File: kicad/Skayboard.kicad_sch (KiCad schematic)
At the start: 13 parts, among them U1 ATmega32U4-M

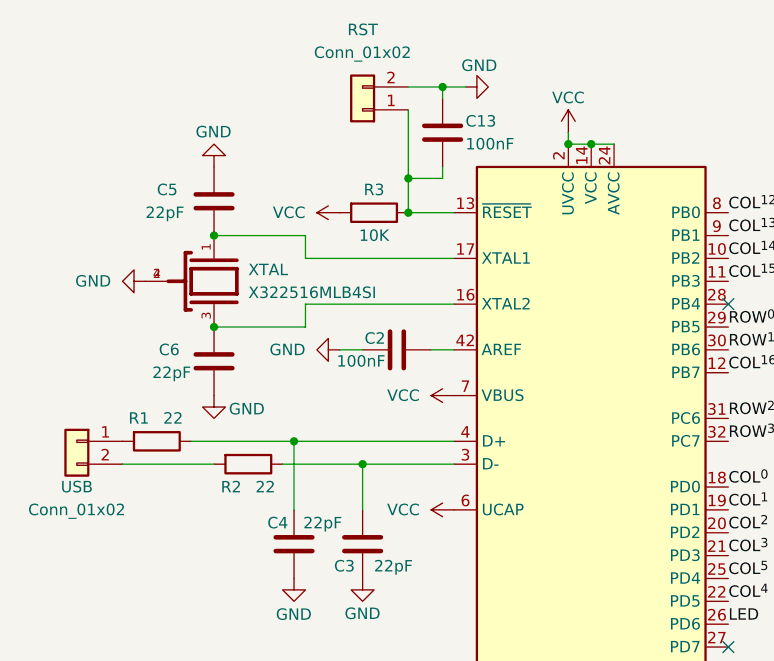
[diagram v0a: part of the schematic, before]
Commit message: fix: adds link for LEDs in README
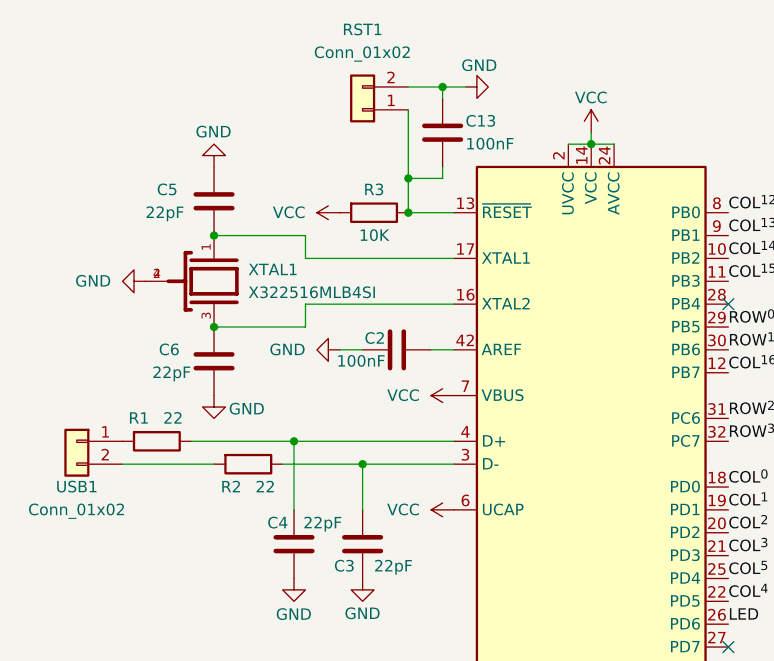
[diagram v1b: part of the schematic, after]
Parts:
- renumbered RST to RST1, USB to USB1, XTAL to XTAL1

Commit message: feat: finishes key layout
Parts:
- added POWER1: Conn_01x02, Connector_Wire:SolderWire-2.5sqmm_1x02_P7.2mm_D2.4mm_OD3.6mm, symbol Connector_Generic:Conn_01x02
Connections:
- net GND: now also POWER1.2 (Pin_2)
- net VCC: now also POWER1.1 (Pin_1)
- no-connect marks 3 -> 4
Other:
- added sheet " (inc/Skey.kicad_sch)
- added sheet , (inc/Skey.kicad_sch)
- added sheet - (inc/Skey.kicad_sch)
- added sheet . (inc/Skey.kicad_sch)
- added sheet 0 (inc/Skey.kicad_sch)
- added sheet 1 (inc/Skey.kicad_sch)
- added sheet 2 (inc/Skey.kicad_sch)
- added sheet 3 (inc/Skey.kicad_sch)
- added sheet 4 (inc/Skey.kicad_sch)
- added sheet 5 (inc/Skey.kicad_sch)
- added sheet 6 (inc/Skey.kicad_sch)
- added sheet 7 (inc/Skey.kicad_sch)
- added sheet 8 (inc/Skey.kicad_sch)
- added sheet 9 (inc/Skey.kicad_sch)
- added sheet ; (inc/Skey.kicad_sch)
- added sheet = (inc/Skey.kicad_sch)
- added sheet A (inc/Skey.kicad_sch)
- added sheet B (inc/Skey.kicad_sch)
- added sheet B Slash (inc/Skey.kicad_sch)
- added sheet Bksp (inc/Skey.kicad_sch)
- added sheet C (inc/Skey.kicad_sch)
- added sheet Caps (inc/Skey.kicad_sch)
- added sheet D (inc/Skey.kicad_sch)
- added sheet Del (inc/Skey.kicad_sch)
- added sheet Down (inc/Skey.kicad_sch)
- added sheet E (inc/Skey.kicad_sch)
- added sheet End (inc/Skey.kicad_sch)
- added sheet Enter (inc/Skey.kicad_sch)
- added sheet Esc (inc/Skey.kicad_sch)
- added sheet F (inc/Skey.kicad_sch)
- added sheet F Slash (inc/Skey.kicad_sch)
- added sheet G (inc/Skey.kicad_sch)
- added sheet H (inc/Skey.kicad_sch)
- added sheet Home (inc/Skey.kicad_sch)
- added sheet I (inc/Skey.kicad_sch)
- added sheet Ins (inc/Skey.kicad_sch)
- added sheet J (inc/Skey.kicad_sch)
- added sheet K (inc/Skey.kicad_sch)
- added sheet L (inc/Skey.kicad_sch)
- added sheet L Alt (inc/Skey.kicad_sch)
- added sheet L Ctrl (inc/Skey.kicad_sch)
- added sheet L Shift (inc/Skey.kicad_sch)
- added sheet L Super (inc/Skey.kicad_sch)
- added sheet Left (inc/Skey.kicad_sch)
- added sheet M (inc/Skey.kicad_sch)
- added sheet Meta (inc/Skey.kicad_sch)
- added sheet N (inc/Skey.kicad_sch)
- added sheet O (inc/Skey.kicad_sch)
- added sheet P (inc/Skey.kicad_sch)
- added sheet PgDn (inc/Skey.kicad_sch)
- added sheet PgUp (inc/Skey.kicad_sch)
- added sheet Q (inc/Skey.kicad_sch)
- added sheet R (inc/Skey.kicad_sch)
- added sheet R Alt (inc/Skey.kicad_sch)
- added sheet R Ctrl (inc/Skey.kicad_sch)
- added sheet R Shift (inc/Skey.kicad_sch)
- added sheet R Super (inc/Skey.kicad_sch)
- added sheet Right (inc/Skey.kicad_sch)
- added sheet S (inc/Skey.kicad_sch)
- added sheet SK1 (inc/Skey.kicad_sch)
- added sheet SK2 (inc/Skey.kicad_sch)
- added sheet SK3 (inc/Skey.kicad_sch)
- added sheet SK4 (inc/Skey.kicad_sch)
- added sheet SK5 (inc/Skey.kicad_sch)
- added sheet Space (inc/Skey.kicad_sch)
- added sheet T (inc/Skey.kicad_sch)
- added sheet Tab (inc/Skey.kicad_sch)
- added sheet U (inc/Skey.kicad_sch)
- added sheet Up (inc/Skey.kicad_sch)
- added sheet V (inc/Skey.kicad_sch)
- added sheet W (inc/Skey.kicad_sch)
- added sheet X (inc/Skey.kicad_sch)
- added sheet Y (inc/Skey.kicad_sch)
- added sheet Z (inc/Skey.kicad_sch)
- added sheet [ (inc/Skey.kicad_sch)
- added sheet ] (inc/Skey.kicad_sch)

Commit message: feat: finishes schematic, starts work on PCB
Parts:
- renumbered C5 to C1, C6 to C2, C4 to C3, C3 to C4, C2 to C5, C13 to C6
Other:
- added sheet ULED1 (inc/LED.kicad_sch)
- added sheet ULED10 (inc/LED.kicad_sch)
- added sheet ULED11 (inc/LED.kicad_sch)
- added sheet ULED12 (inc/LED.kicad_sch)
- added sheet ULED13 (inc/LED.kicad_sch)
- added sheet ULED14 (inc/LED.kicad_sch)
- added sheet ULED15 (inc/LED.kicad_sch)
- added sheet ULED16 (inc/LED.kicad_sch)
- added sheet ULED17 (inc/LED.kicad_sch)
- added sheet ULED18 (inc/LED.kicad_sch)
- added sheet ULED19 (inc/LED.kicad_sch)
- added sheet ULED2 (inc/LED.kicad_sch)
- added sheet ULED20 (inc/LED.kicad_sch)
- added sheet ULED21 (inc/LED.kicad_sch)
- added sheet ULED22 (inc/LED.kicad_sch)
- added sheet ULED23 (inc/LED.kicad_sch)
- added sheet ULED24 (inc/LED.kicad_sch)
- added sheet ULED25 (inc/LED.kicad_sch)
- added sheet ULED26 (inc/LED.kicad_sch)
- added sheet ULED27 (inc/LED.kicad_sch)
- added sheet ULED28 (inc/LED.kicad_sch)
- added sheet ULED29 (inc/LED.kicad_sch)
- added sheet ULED3 (inc/LED.kicad_sch)
- added sheet ULED30 (inc/LED.kicad_sch)
- added sheet ULED31 (inc/LED.kicad_sch)
- added sheet ULED32 (inc/LED.kicad_sch)
- added sheet ULED33 (inc/LED.kicad_sch)
- added sheet ULED34 (inc/LED.kicad_sch)
- added sheet ULED35 (inc/LED.kicad_sch)
- added sheet ULED36 (inc/LED.kicad_sch)
- added sheet ULED37 (inc/LED.kicad_sch)
- added sheet ULED38 (inc/LED.kicad_sch)
- added sheet ULED39 (inc/LED.kicad_sch)
- added sheet ULED4 (inc/LED.kicad_sch)
- added sheet ULED40 (inc/LED.kicad_sch)
- added sheet ULED41 (inc/LED.kicad_sch)
- added sheet ULED42 (inc/LED.kicad_sch)
- added sheet ULED43 (inc/LED.kicad_sch)
- added sheet ULED44 (inc/LED.kicad_sch)
- added sheet ULED45 (inc/LED.kicad_sch)
- added sheet ULED5 (inc/LED.kicad_sch)
- added sheet ULED6 (inc/LED.kicad_sch)
- added sheet ULED7 (inc/LED.kicad_sch)
- added sheet ULED8 (inc/LED.kicad_sch)
- added sheet ULED9 (inc/LED.kicad_sch)
- moved on the sheet: C1, C2, C3, C4, C5, C6, POWER1, R1, R2, R3, RST1, U1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

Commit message: Outro - M83
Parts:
- removed C4: 22pF, Capacitor_SMD:C_01005_0402Metric, symbol Device:C
- removed U1: ATmega32U4-M, Package_DFN_QFN:QFN-44-1EP_7x7mm_P0.5mm_EP5.2x5.2mm, symbol MCU_Microchip_ATmega:ATmega32U4-M
- removed XTAL1: X322516MLB4SI, OSC_X322516MLB4SI, symbol YSX321SL:X322516MLB4SI
- added C127, C128, C6: 100nF, Capacitor_SMD:C_0402_1005Metric_Pad0.74x0.62mm_HandSolder, symbol Device:C
- added U1: ATmega32U4-A, Package_QFP:TQFP-44_10x10mm_P0.8mm, symbol MCU_Microchip_ATmega:ATmega32U4-A
- added Y1: 16MHz, Crystal:Crystal_HC49-U_Vertical, symbol Device:Crystal
- C1: renamed from C6; footprint Capacitor_SMD:C_0402_1005Metric -> Capacitor_SMD:C_0402_1005Metric_Pad0.74x0.62mm_HandSolder
- C2: renamed from C1; footprint Capacitor_SMD:C_01005_0402Metric -> Capacitor_SMD:C_0402_1005Metric_Pad0.74x0.62mm_HandSolder
- C3: value 22pF -> 1uF; footprint Capacitor_SMD:C_01005_0402Metric -> Capacitor_SMD:C_0603_1608Metric_Pad1.08x0.95mm_HandSolder
- C4: renamed from C2; footprint Capacitor_SMD:C_01005_0402Metric -> Capacitor_SMD:C_0402_1005Metric_Pad0.74x0.62mm_HandSolder
- C5: value 100nF -> 10uF; footprint Capacitor_SMD:C_01005_0402Metric -> Capacitor_SMD:C_0603_1608Metric_Pad1.08x0.95mm_HandSolder
- POWER1, RST1, USB1: now not fitted
- R1: renamed from R3; footprint Resistor_SMD:R_0201_0603Metric -> Resistor_SMD:R_0603_1608Metric_Pad0.98x0.95mm_HandSolder
- R2: renamed from R1; footprint Resistor_SMD:R_0201_0603Metric -> Resistor_SMD:R_0603_1608Metric_Pad0.98x0.95mm_HandSolder
- R3: renamed from R2; footprint Resistor_SMD:R_0201_0603Metric -> Resistor_SMD:R_0603_1608Metric_Pad0.98x0.95mm_HandSolder
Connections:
- net COL^{0}: now also U1.18 (PD0)
- net COL^{10}: now also U1.38 (PF5)
- net COL^{11}: now also U1.37 (PF6)
- net COL^{12}: now also U1.32 (PC7)
- net COL^{13}: now also U1.36 (PF7)
- net COL^{14}: now also U1.30 (PB6)
- net COL^{15}: now also U1.31 (PC6)
- net COL^{16}: now also U1.39 (PF4)
- net COL^{1}: now also U1.19 (PD1)
- net COL^{2}: now also U1.20 (PD2)
- net COL^{3}: now also U1.21 (PD3)
- net COL^{4}: now also U1.22 (PD5)
- net COL^{5}: now also U1.25 (PD4)
- net COL^{6}: now also U1.26 (PD6)
- net COL^{7}: now also U1.1 (PE6)
- net COL^{8}: now also U1.41 (PF0)
- net COL^{9}: now also U1.40 (PF1)
- net GND: now also C127.2, C128.2, C6.2, U1.15 (GND), U1.23 (GND), U1.35 (GND), U1.43 (GND), U1.5 (UGND); no longer C3.1
- net LED: now also U1.29 (PB5)
- net ROW^{0}: now also U1.10 (PB2)
- net ROW^{1}: now also U1.9 (PB1)
- net ROW^{2}: now also U1.8 (PB0)
- net ROW^{3}: now also U1.11 (PB3)
- net ROW^{4}: now also U1.12 (PB7)
- net VCC: now also C3.1, C5.2, C127.1, C128.1, C6.1, U1.14 (VCC), U1.2 (UVCC), U1.24 (AVCC), U1.34 (VCC), U1.42 (AREF), U1.44 (AVCC), U1.7 (VBUS)
- net at C1.2, R1.1, RST1.1 (Pin_1): now also U1.13 (~{RESET})
- net at C4.2: now also U1.16 (XTAL2), Y1.1
- net at C2.2: now also U1.17 (XTAL1), Y1.2
- net at R3.1: now also U1.3 (D-)
- net at C3.2: now also U1.6 (UCAP); no longer R2.1
- new net: R2.1, U1.4 (D+)
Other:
- removed sheet ULED45
- note added: "sorry"
- moved on the sheet: C2, C4, R2, R3
